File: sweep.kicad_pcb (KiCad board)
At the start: 2 copper layers, 216.9 x 86.9 mm, 216 parts, among them J1 USB_C_Receptacle_USB2.0_16P, J10 Conn_01x12, J11 Conn_01x01, J12 Conn_01x01, J13 Conn_01x01, J2 Conn_01x01, J3 USB_C_Receptacle_USB2.0_16P, J4 USB_C_Receptacle_USB2.0_16P, J5 USB_C_Receptacle_USB2.0_16P, J7 Conn_01x05, J8 Conn_01x05, J9 Conn_01x12, SW1 SW_Push, SW10 SW_Push, SW11 SW_Push, SW12 SW_Push, SW13 SW_Push, SW14 SW_Push, SW15 SW_Push, SW16 SW_Push, SW17 SW_Push, SW18 SW_Push, SW19 SW_Push, SW2 SW_Push, SW20 SW_Push, SW21 SW_Push, SW22 SW_Push, SW23 SW_Push, SW24 SW_Push, SW25 SW_Push, SW26 SW_Push, SW27 SW_Push, SW28 SW_Push, SW29 SW_Push, SW3 SW_Push, SW30 SW_Push, SW31 SW_Push, SW32 SW_Push, SW33 SW_Push, SW34 SW_Push, SW35 SW_Push, SW36 SW_Push, SW37 SW_Push, SW38 SW_Push, SW4 SW_Push, SW5 SW_Push, SW6 SW_Push, SW7 SW_Push, SW8 SW_Push, SW9 SW_Push, U1 RP2040, U10 SN74LVC1T45DRL, U2 XC6206PxxxMR, U3 SRV05-4, U4 W25Q128JVS, U5 RP2040, U6 SRV05-4, U7 XC6206PxxxMR, U8 W25Q128JVS, U9 SN74LVC1T45DRL, Y1 Crystal_GND24, Y2 Crystal_GND24

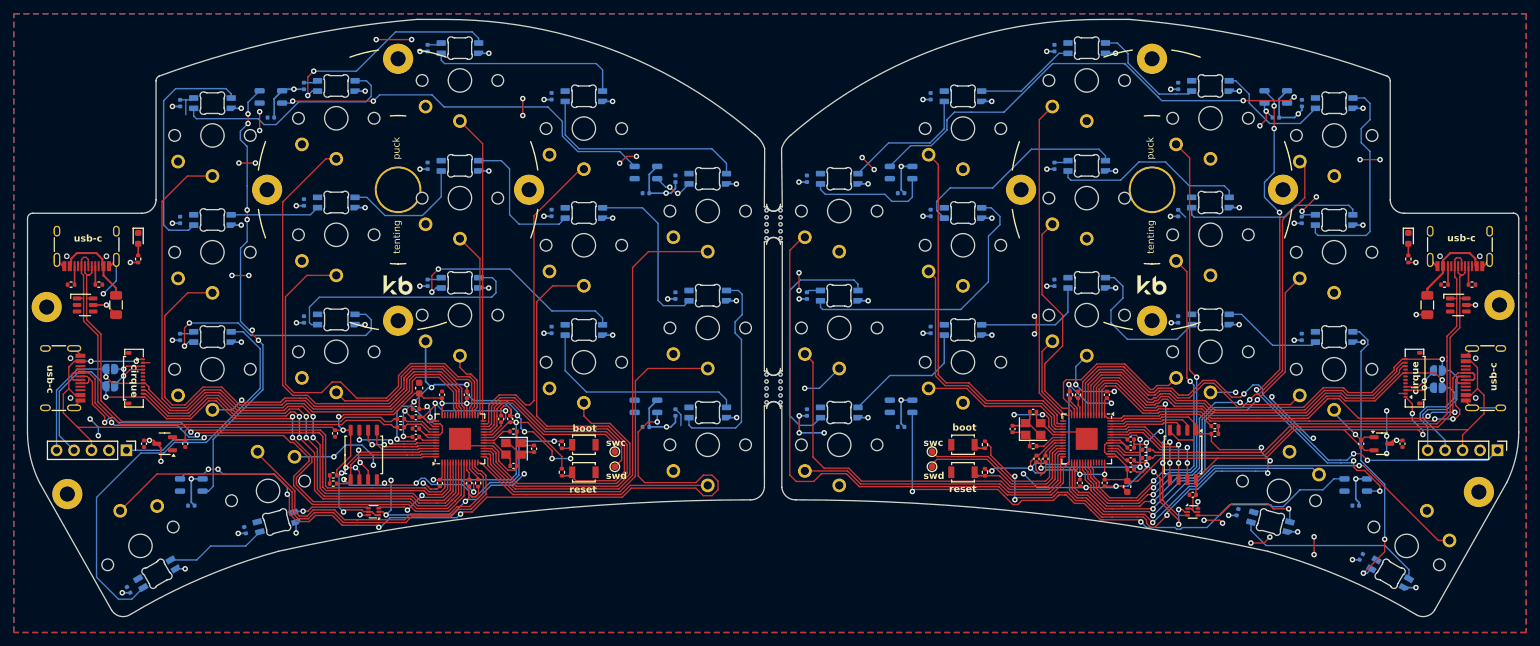
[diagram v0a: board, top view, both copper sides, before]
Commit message: Add silkscreen graphics
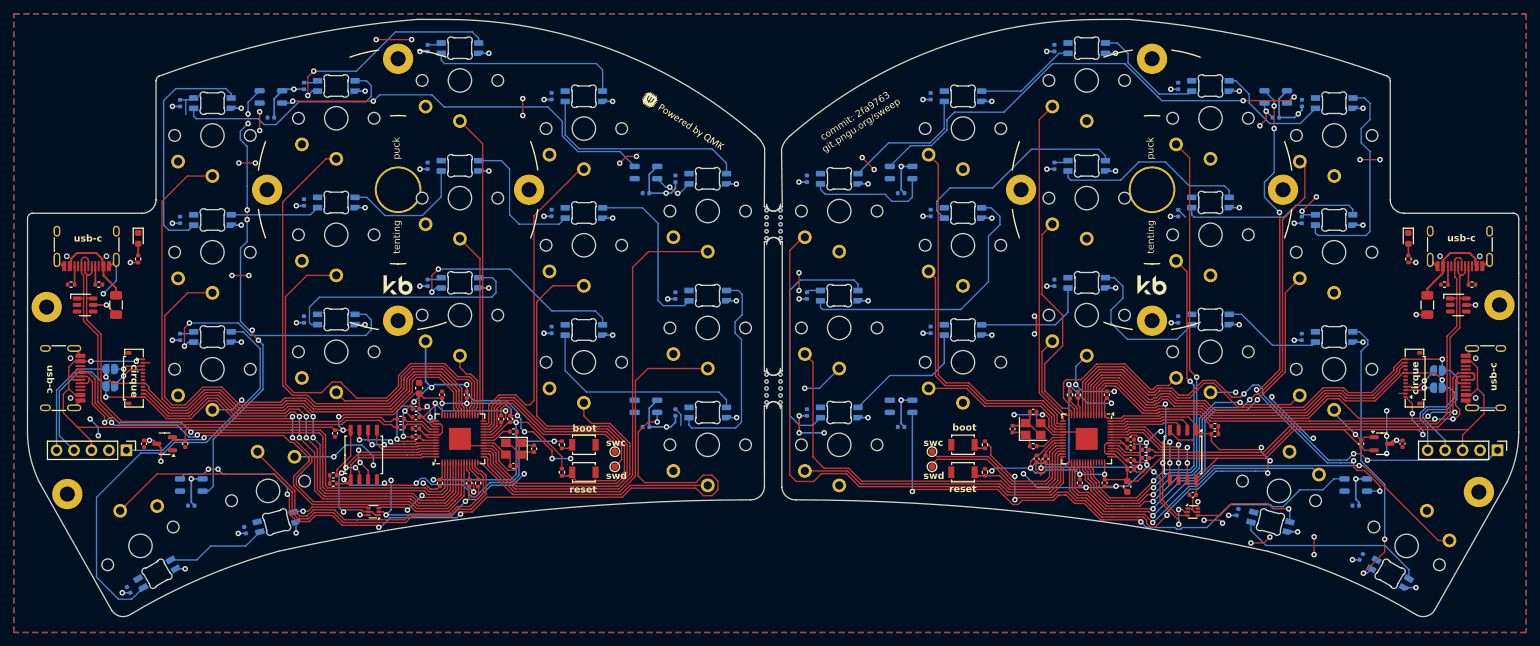
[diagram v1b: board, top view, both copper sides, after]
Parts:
- added G***: LOGO, LOGO, F.Cu at (137.4, 65.7)
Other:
- board text added: "commit: 2fa9763 git.pngu.org/sweep"

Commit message: Adds updated PCBs (see changelog) and production files
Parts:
- removed J10, J9: Conn_01x12, PCM_marbastlib-various:CON_FH33J-12S-0.5SH
- removed J8: Conn_01x05, Connector_PinHeader_2.54mm:PinHeader_1x05_P2.54mm_Vertical
- removed JP1, JP2, JP3, JP4: SolderJumper_2_Open, Jumper:SolderJumper-2_P1.3mm_Open_RoundedPad1.0x1.5mm
- removed the REF** at (256.1, 92.4)
- removed the REF** at (253.1, 119.6)
- removed the REF** at (47.8, 119.9)
- removed the REF** at (44.8, 92.7)
- added C75: 100n, Capacitor_SMD:C_0402_1005Metric, F.Cu at (242.4, 99.2)
- added C76: 100n, Capacitor_SMD:C_0402_1005Metric, F.Cu at (59.0, 99.2)
- added J6: Conn_01x08, Connector_FFC-FPC:TE_0-1734839-8_1x08-1MP_P0.5mm_Horizontal, F.Cu at (251.5, 115.2)
- added R23: 0.005, Resistor_SMD:R_1206_3216Metric, F.Cu at (245.6, 96.3)
- added R24: 75k, Resistor_SMD:R_0402_1005Metric, F.Cu at (245.0, 103.1)
- added R25: 75k, Resistor_SMD:R_0402_1005Metric, F.Cu at (246.2, 103.1)
- added R26: 0.005, Resistor_SMD:R_1206_3216Metric, F.Cu at (55.8, 96.3)
- added R27: 75k, Resistor_SMD:R_0402_1005Metric, F.Cu at (56.4, 103.1)
- added R28: 75k, Resistor_SMD:R_0402_1005Metric, F.Cu at (55.2, 103.1)
- added REF**: MountingHole_2.2mm_M2, MountingHole:MountingHole_2.2mm_M2, F.Cu at (252.8, 120.1)
- added REF**: MountingHole_2.2mm_M2, MountingHole:MountingHole_2.2mm_M2, F.Cu at (57.1, 115.0)
- added REF**: MountingHole_2.2mm_M2, MountingHole:MountingHole_2.2mm_M2, F.Cu at (48.1, 120.1)
- added REF**: MountingHole_2.2mm_M2, MountingHole:MountingHole_2.2mm_M2, F.Cu at (243.8, 115.0)
- added U11: INA138, Package_TO_SOT_SMD:SOT-23-5, F.Cu at (245.6, 99.7)
- added U12: INA138, Package_TO_SOT_SMD:SOT-23-5, F.Cu at (55.8, 99.7)
- J7: value Conn_01x05 -> Conn_01x08; footprint Connector_PinHeader_2.54mm:PinHeader_1x05_P2.54mm_Vertical -> Connector_FFC-FPC:TE_0-1734839-8_1x08-1MP_P0.5mm_Horizontal
- moved J7 206.4 mm to (49.5, 115.2), turned to 180 degrees
- moved C1 10.7 mm to (242.3, 101.8), turned to 0 degrees
- moved C20 10.7 mm to (59.1, 101.8), turned to 180 degrees
- moved U2 8.37 mm to (242.3, 104.8), turned to 90 degrees
- moved U7 8.20 mm to (59.1, 104.8), turned to 90 degrees
- moved C2 7.86 mm to (242.3, 107.8), turned to 180 degrees
- moved C23 7.50 mm to (59.1, 107.8), turned to 180 degrees
- moved C6 0.70 mm to (199.4, 118.2)
- moved C9 0.10 mm to (188.7, 114.7)
- moved C59 0.10 mm to (190.0, 114.7)
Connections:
- F1 pad 2: +5V -> Net-(U11-+)
- F2 pad 2: +5V -> Net-(U12-+)
- J7 pad 1: LCD_CS_L -> LCD_BL_R
- J7 pad 3: +3V3 -> LCD_RST_R
- J7 pad 4: SCK_L -> SPI_MISO_R
- J7 pad 5: MOSI_L -> SPI_MOSI_R
- U1 pad 38: unconnected-(U1-GPIO26_ADC0-Pad38) -> CURR_MEAS_L
- U1 pad 39: unconnected-(U1-GPIO27_ADC1-Pad39) -> VOLT_MEAS_L
- U1 pad 40: unconnected-(U1-GPIO28_ADC2-Pad40) -> LCD_RST_L
- U1 pad 5: MOSI_L -> SPI_MOSI_L
- U1 pad 6: CIRQUE_CS_L -> SPI_MISO_L
- U1 pad 7: MISO_L -> LCD_CS_L
- U1 pad 8: SCK_L -> SPI_SCK_L
- U1 pad 9: LCD_CS_L -> LCD_BL_L
- U5 pad 32: SW14_R -> SW4_R
- U5 pad 34: SW4_R -> SW15_R
- U5 pad 35: SW15_R -> SW14_R
- U5 pad 38: unconnected-(U5-GPIO26_ADC0-Pad38) -> CURR_MEAS_R
- U5 pad 39: unconnected-(U5-GPIO27_ADC1-Pad39) -> VOLT_MEAS_R
- U5 pad 40: unconnected-(U5-GPIO28_ADC2-Pad40) -> LCD_RST_R
- U5 pad 5: MOSI_R -> SPI_MOSI_R
- U5 pad 6: CIRQUE_CS_R -> SPI_MISO_R
- U5 pad 7: MISO_R -> LCD_CS_R
- U5 pad 8: SCK_R -> SPI_SCK_R
- U5 pad 9: LCD_CS_R -> LCD_BL_R
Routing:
- net SCK_R: track 93.5 -> 0.00 mm, vias 3 -> 0
- net MOSI_R: track 89.4 -> 0.00 mm, vias 3 -> 0
- net SCK_L: track 85.5 -> 0.00 mm, vias 1 -> 0
- net VOLT_MEAS_L: track 0.00 -> 82.6 mm, vias 0 -> 6
- net LCD_BL_L: track 0.00 -> 79.6 mm, vias 0 -> 4
- net MOSI_L: track 77.6 -> 0.00 mm, vias 1 -> 0
- net CURR_MEAS_L: track 0.00 -> 74.7 mm, vias 0 -> 4
- net LCD_RST_L: track 0.00 -> 73.9 mm, vias 0 -> 4
- net SPI_SCK_L: track 0.00 -> 73.9 mm, vias 0 -> 2
- net SPI_SCK_R: track 0.00 -> 73.7 mm, vias 0 -> 2
- net SPI_MISO_L: track 0.00 -> 72.6 mm, vias 0 -> 2
- net SPI_MISO_R: track 0.00 -> 71.8 mm, vias 0 -> 2
- net LCD_RST_R: track 0.00 -> 71.3 mm, vias 0 -> 7
- net SPI_MOSI_L: track 0.00 -> 70.9 mm, vias 0 -> 2
- net SPI_MOSI_R: track 0.00 -> 69.5 mm, vias 0 -> 2
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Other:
- board text added: "lcd"
- board text removed: "cirque"

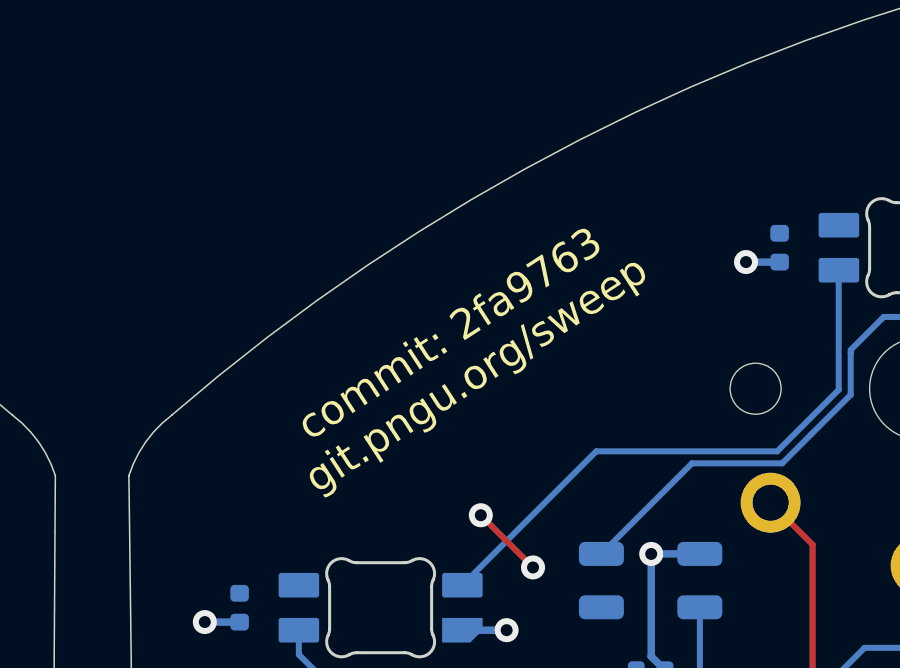
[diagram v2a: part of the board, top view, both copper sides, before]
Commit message: Update silkscreen graphics, interactive bom, and svg's
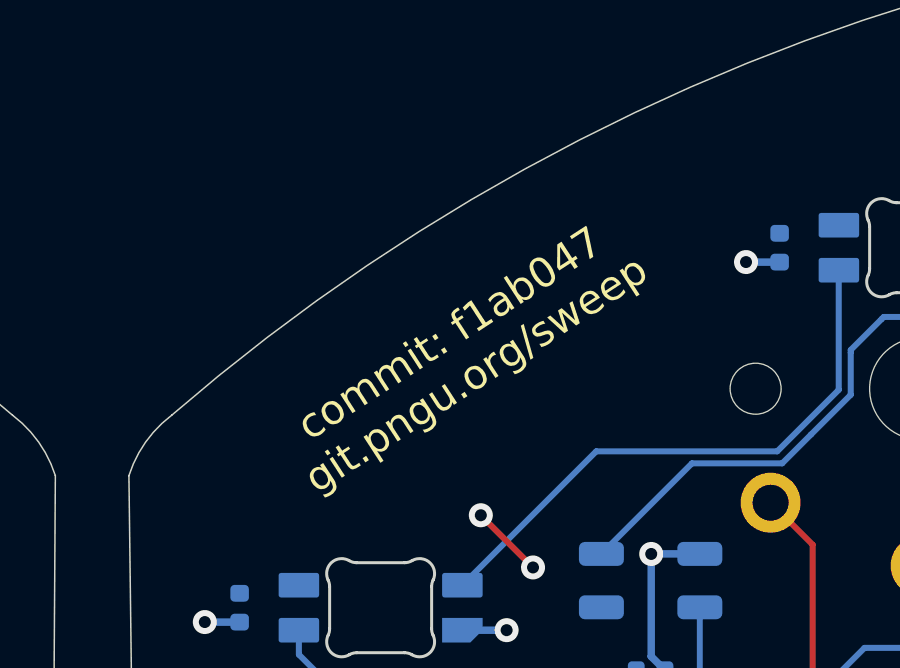
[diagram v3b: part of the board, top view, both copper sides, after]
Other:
- board text added: "commit: f1ab047 git.pngu.org/sweep"
- board text removed: "commit: 2fa9763 git.pngu.org/sweep"
